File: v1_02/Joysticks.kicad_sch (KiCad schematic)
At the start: 29 parts, among them J10 DB9_Male_MountingHoles, J11 DA15_Socket_MountingHoles, J13 Aliexpress ADS1115 module, J15 Conn_01x01_Pin, J17 Conn_01x03_Pin, U4 74LV165A, U5 74LV165A, U6 LM4040D20ILPR, U7 PCF8583T, Y1 32.768 kHz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

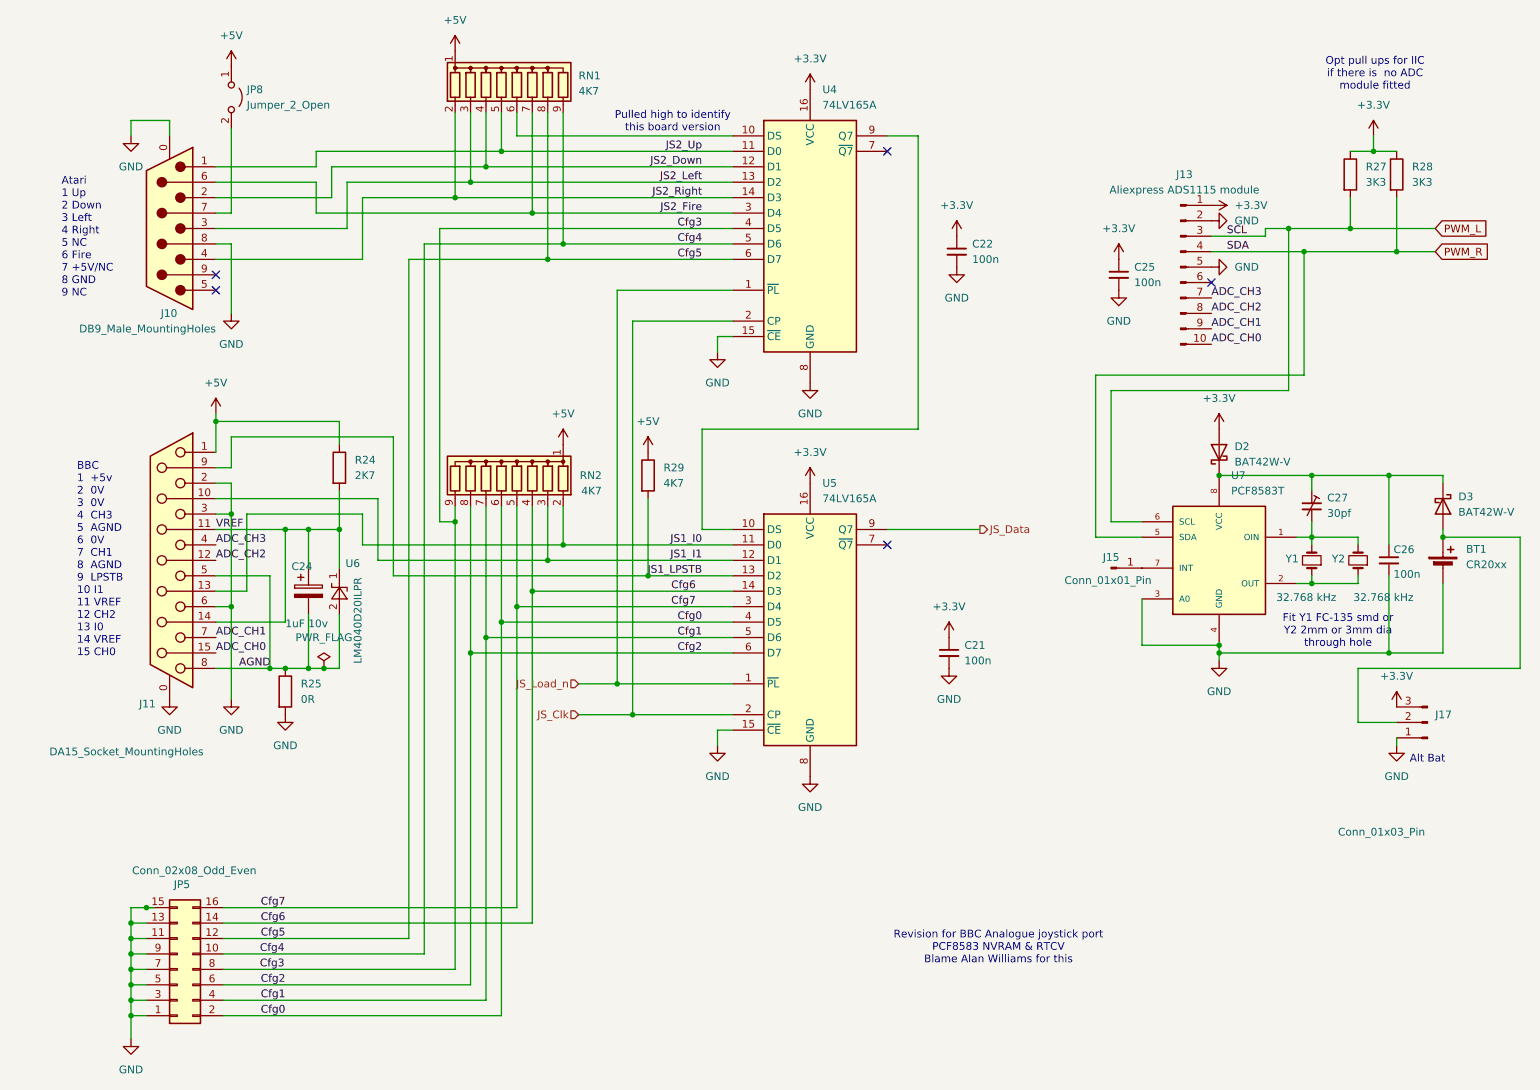
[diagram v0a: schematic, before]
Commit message: v1_02: Fix some ERC warnings
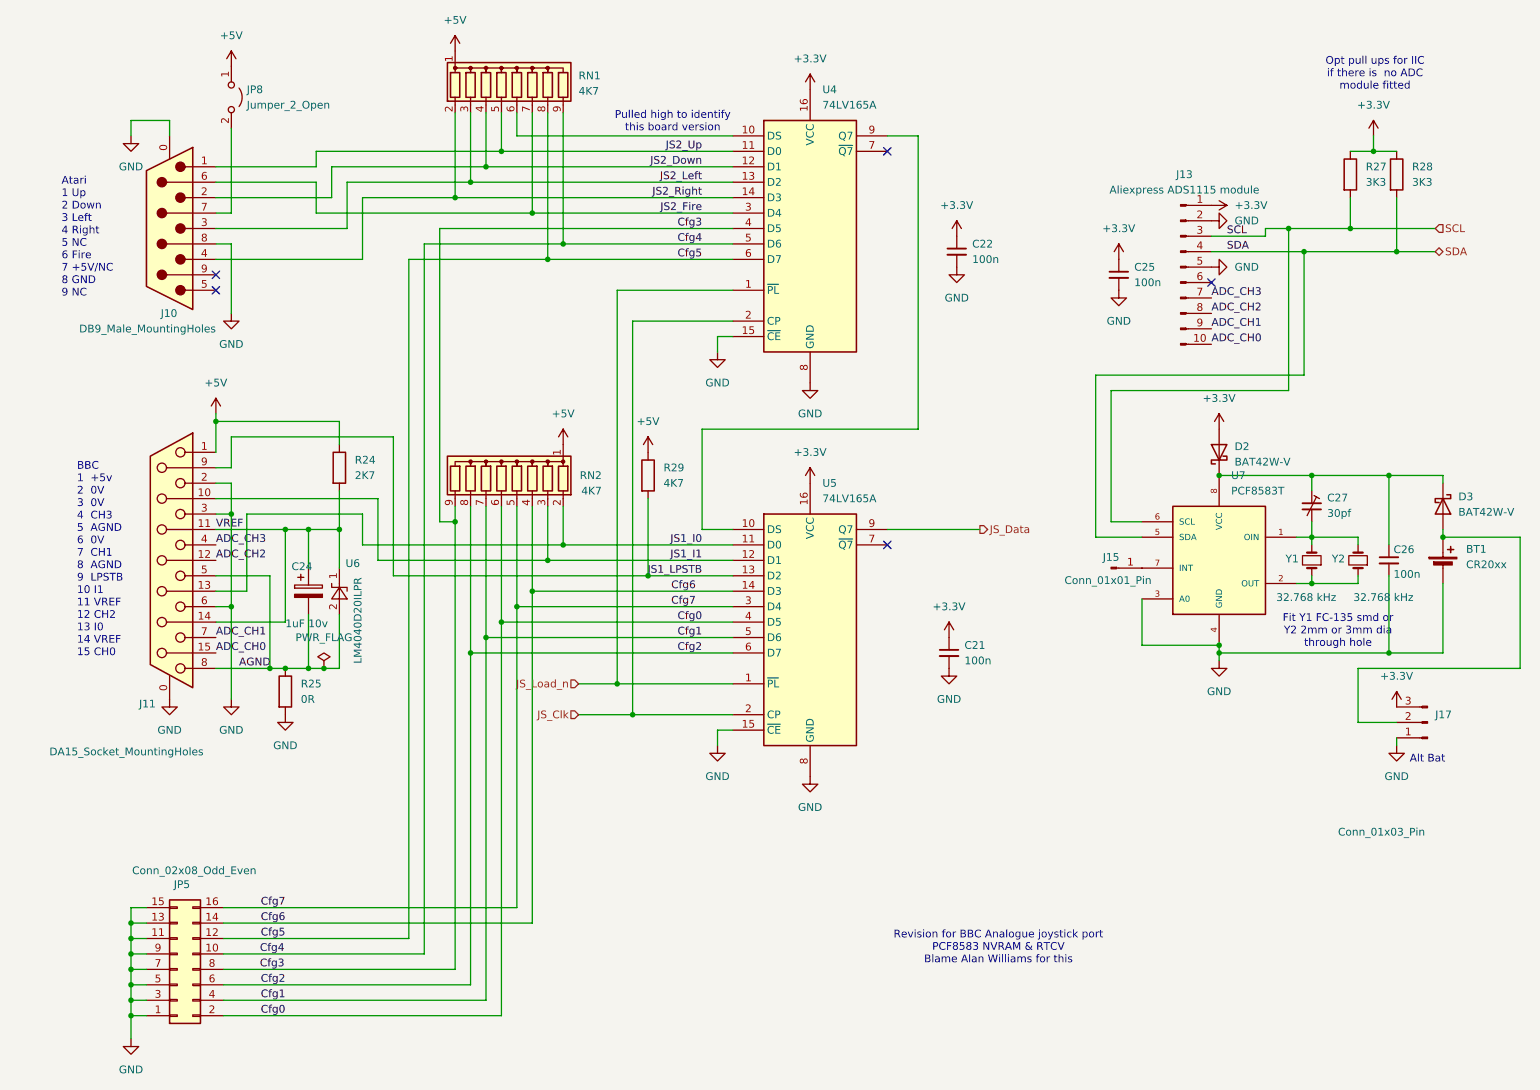
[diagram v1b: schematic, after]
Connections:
- net AGND: now reaches C24.2, J11.5, J11.8, R25.1, U6.2 (A)
- net PWM_L renamed SCL
- net PWM_R renamed SDA
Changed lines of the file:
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@@
+	)
+	(junction
+		(at 248.92 110.49)
+		(diameter 0)
+		(color 0 0 0 0)
+	)
+	(junction
+		(at 134.62 127)
+		(diameter 0)
+		(color 0 0 0 0)
+	)
+	(junction
+		(at 125.73 104.14)
+		(diameter 0)
+		(color 0 0 0 0)
+	)
+	(junction
+		(at 86.36 124.46)
+		(diameter 0)
+		(color 0 0 0 0)
+	)
+	(junction
+		(at 71.12 114.3)
+		(diameter 0)
+		(color 0 0 0 0)
+	)
+	(junction
+		(at 120.65 49.53)
+		(diameter 0)
+		(color 0 0 0 0)
+	)
+	(junction
+		(at 107.95 46.99)
+		(diameter 0)
+		(color 0 0 0 0)
+	)
+	(junction
+		(at 137.16 132.08)
+		(diameter 0)
+		(color 0 0 0 0)
 	)
 	(junction
@@
 	)
 	(junction
-		(at 248.92 110.49)
-		(diameter 0)
-		(color 0 0 0 0)
-	)
-	(junction
-		(at 134.62 127)
-		(diameter 0)
-		(color 0 0 0 0)
-	)
-	(junction
-		(at 125.73 104.14)
-		(diameter 0)
-		(color 0 0 0 0)
-	)
-	(junction
-		(at 86.36 124.46)
-		(diameter 0)
-		(color 0 0 0 0)
-	)
-	(junction
-		(at 71.12 114.3)
-		(diameter 0)
-		(color 0 0 0 0)
-	)
-	(junction
-		(at 120.65 49.53)
-		(diameter 0)
-		(color 0 0 0 0)
-	)
-	(junction
-		(at 107.95 46.99)
-		(diameter 0)
-		(color 0 0 0 0)
-	)
-	(junction
-		(at 137.16 132.08)
-		(diameter 0)
-		(color 0 0 0 0)
-	)
-	(junction
 		(at 54.61 181.61)
 		(diameter 0)
@@
 	(junction
 		(at 54.61 176.53)
-		(diameter 0)
-		(color 0 0 0 0)
-	)
-	(junction
-		(at 57.15 163.83)
 		(diameter 0)
 		(color 0 0 0 0)
@@
 	(wire
 		(pts
+			(xy 68.58 124.46) (xy 77.47 124.46)
+		)
+		(stroke
+			(width 0)
+			(type default)
+		)
+	)
+	(wire
+		(pts
 			(xy 107.95 97.79) (xy 107.95 100.33)
 		)
@@
 	(wire
 		(pts
-			(xy 68.58 124.46) (xy 77.47 124.46)
-		)
-		(stroke
-			(width 0)
-			(type default)
-		)
-	)
-	(wire
-		(pts
 			(xy 69.85 176.53) (xy 110.49 176.53)
 		)
@@
 		(pts
 			(xy 125.73 104.14) (xy 153.67 104.14)
-		)
-		(stroke
-			(width 0)
-			(type default)
-		)
-	)
-	(wire
-		(pts
-			(xy 58.42 163.83) (xy 57.15 163.83)
 		)
 		(stroke
@@
 		)
 	)
-	(label ""
-		(at 81.28 124.46 0)
-		(effects
-			(font
-				(size 1.27 1.27)
-			)
-			(justify left bottom)
-		)
-	)
 	(label "Cfg0"
 		(at 80.01 181.61 180)
@@
 			)
 			(justify right bottom)
-		)
-	)
-	(global_label "PWM_R"
-		(shape input)
-		(at 269.24 55.88 0)
-		(fields_autoplaced yes)
-		(effects
-			(font
-				(size 1.27 1.27)
-			)
-			(justify left)
-		)
-		(property "Intersheetrefs" "${INTERSHEET_REFS}"
-			(at 278.6356 55.88 0)
-			(effects
-				(font
-					(size 1.27 1.27)
-				)
-				(justify left)
-				(hide yes)
-			)
-		)
-	)
-	(global_label "PWM_L"
-		(shape input)
-		(at 269.24 52.07 0)
-		(fields_autoplaced yes)
-		(effects
-			(font
-				(size 1.27 1.27)
-			)
-			(justify left)
-		)
-		(property "Intersheetrefs" "${INTERSHEET_REFS}"
-			(at 278.3937 52.07 0)
-			(effects
-				(font
-					(size 1.27 1.27)
-				)
-				(justify left)
-				(hide yes)
-			)
 		)
 	)
@@
 		)
 	)
+	(hierarchical_label "SDA"
+		(shape bidirectional)
+		(at 269.24 55.88 0)
+		(effects
+			(font
+				(size 1.27 1.27)
+			)
+			(justify left)
+		)
+	)
 	(hierarchical_label "JS_Clk"
 		(shape input)
@@
 		)
 	)
+	(hierarchical_label "SCL"
+		(shape input)
+		(at 269.24 52.07 0)
+		(effects
+			(font
+				(size 1.27 1.27)
+			)
+			(justify left)
+		)
+	)

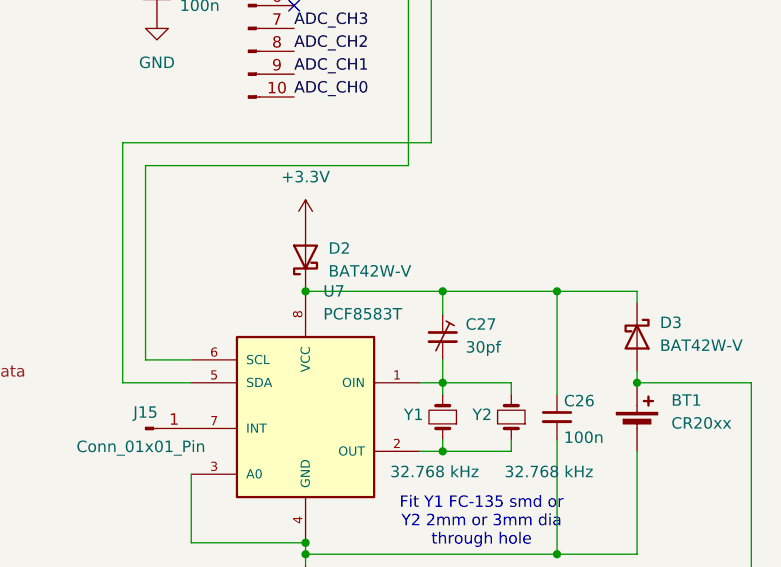
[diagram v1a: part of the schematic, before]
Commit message: v1_02: Updated symbols/footprints for KiCAD9; fix all ERC/DRC warnings
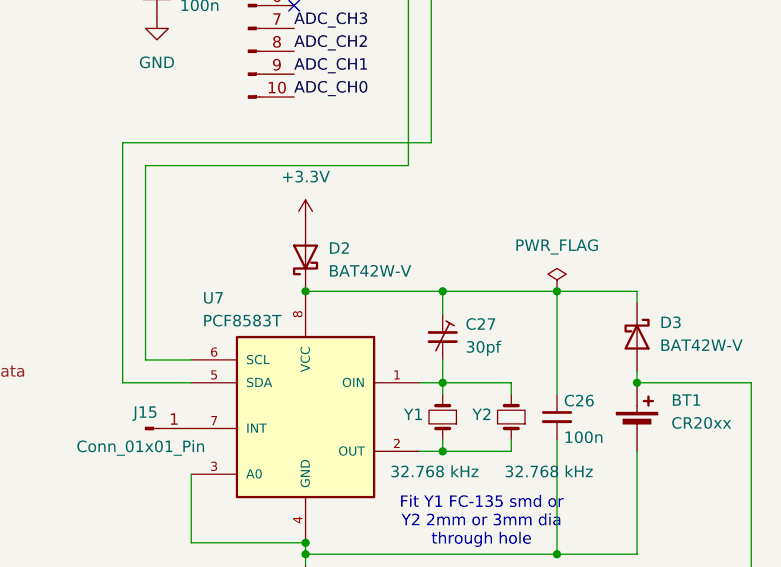
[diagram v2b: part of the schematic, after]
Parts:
- J10: symbol Connector:DB9_Male_MountingHoles -> Connector:DE9_Pins_MountingHoles
- U7: symbol PCF8583:PCF8583 -> TangNano20k:PCF8583
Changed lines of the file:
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@@
 			)
 		)
-		(property "Description" ""
+		(property "Description" "Power symbol creates a global label with name \"GND\" , ground"
 			(at 166.37 142.24 0)
 			(effects
@@
 			)
 		)
-		(property "Description" ""
+		(property "Description" "Power symbol creates a global label with name \"GND\" , ground"
 			(at 80.01 132.08 0)
 			(effects
@@
 			)
 		)
-		(property "Description" ""
+		(property "Description" "Power symbol creates a global label with name \"GND\" , ground"
 			(at 60.96 129.54 0)
 			(effects
@@
 			)
 		)
-		(property "Description" ""
+		(property "Description" "Power symbol creates a global label with name \"+3.3V\""
 			(at 262.89 130.81 0)
 			(effects
@@
 			)
 		)
-		(property "Description" ""
+		(property "Description" "Power symbol creates a global label with name \"GND\" , ground"
 			(at 262.89 137.16 0)
 			(effects
@@
 			)
 		)
-		(property "Description" ""
+		(property "Description" "Power symbol creates a global label with name \"+3.3V\""
 			(at 217.17 57.15 0)
 			(effects
@@
 			)
 		)
-		(property "Description" ""
+		(property "Description" "Power symbol creates a global label with name \"GND\" , ground"
 			(at 233.68 123.19 0)
 			(effects
@@
 			)
 		)
-		(property "Description" ""
+		(property "Description" "Power symbol creates a global label with name \"GND\" , ground"
 			(at 151.13 72.39 0)
 			(effects
@@
 			)
 		)
-		(property "Description" ""
+		(property "Description" "Power symbol creates a global label with name \"+5V\""
 			(at 71.12 25.4 0)
 			(effects
@@
 			)
 		)
-		(property "Description" ""
+		(property "Description" "Power symbol creates a global label with name \"+3.3V\""
 			(at 166.37 93.98 0)
 			(effects
@@
 			)
 		)
-		(property "Description" ""
+		(property "Description" "Power symbol creates a global label with name \"+3.3V\""
 			(at 259.08 36.83 0)
 			(effects
@@
 			)
 		)
-		(property "Description" ""
+		(property "Description" "Power symbol creates a global label with name \"GND\" , ground"
 			(at 232.41 50.8 0)
 			(effects
@@
 			)
 		)
-		(property "Description" ""
+		(property "Description" "Power symbol creates a global label with name \"+3.3V\""
 			(at 232.41 48.26 0)
 			(effects
@@
 			)
 		)
-		(property "Description" ""
+		(property "Description" "Power symbol creates a global label with name \"GND\" , ground"
 			(at 232.41 58.42 0)
 			(effects
@@
 			)
 		)
-		(property "Description" ""
+		(property "Description" "Power symbol creates a global label with name \"+3.3V\""
 			(at 166.37 29.21 0)
 			(effects
@@
 			)
 		)
-		(property "Description" ""
+		(property "Description" "Power symbol creates a global label with name \"GND\" , ground"
 			(at 54.61 185.42 0)
 			(effects
@@
 			)
 		)
-		(property "Description" ""
+		(property "Description" "Power symbol creates a global label with name \"+3.3V\""
 			(at 190.5 53.34 0)
 			(effects
@@
 			)
 		)
-		(property "Description" ""
+		(property "Description" "Power symbol creates a global label with name \"GND\" , ground"
 			(at 217.17 62.23 0)
 			(effects
@@
 			)
 		)
-		(property "Description" ""
+		(property "Description" "Power symbol creates a global label with name \"GND\" , ground"
 			(at 71.12 129.54 0)
 			(effects
@@
 			)
 		)
-		(property "Description" ""
+		(property "Description" "Power symbol creates a global label with name \"+5V\""
 			(at 139.7 88.9 0)
 			(effects
@@
 			)
 		)
-		(property "Description" ""
+		(property "Description" "Power symbol creates a global label with name \"+3.3V\""
 			(at 189.23 119.38 0)
 			(effects
@@
 			)
 		)
-		(property "Description" ""
+		(property "Description" "Power symbol creates a global label with name \"GND\" , ground"
 			(at 189.23 124.46 0)
 			(effects
@@
 			)
 		)
-		(property "Description" ""
+		(property "Description" "Power symbol creates a global label with name \"GND\" , ground"
 			(at 151.13 137.16 0)
 			(effects
@@
 			)
 		)
-		(property "Description" ""
+		(property "Description" "Power symbol creates a global label with name \"+5V\""
 			(at 68.58 82.55 0)
 			(effects
@@
 	)
 	(symbol
+		(lib_id "power:PWR_FLAG")
+		(at 261.62 92.71 0)
+		(unit 1)
+		(exclude_from_sim no)
+		(in_bom yes)
+		(on_board yes)
+		(dnp no)
+		(fields_autoplaced yes)
+		(property "Reference" "#FLG02"
+			(at 261.62 90.805 0)
+			(effects
+				(font
+					(size 1.27 1.27)
+				)
+				(hide yes)
+			)
+		)
+		(property "Value" "PWR_FLAG"
+			(at 261.62 87.63 0)
+			(effects
+				(font
+					(size 1.27 1.27)
+				)
+			)
+		)
+		(property "Footprint" ""
+			(at 261.62 92.71 0)
+			(effects
+				(font
+					(size 1.27 1.27)
+				)
+				(hide yes)
+			)
+		)
+		(property "Datasheet" "~"
+			(at 261.62 92.71 0)
+			(effects
+				(font
+					(size 1.27 1.27)
+				)
+				(hide yes)
+			)
+		)
+		(property "Description" "Special symbol for telling ERC where power comes from"
+			(at 261.62 92.71 0)
+			(effects
+				(font
+					(size 1.27 1.27)
+				)
+				(hide yes)
+			)
+		)
+		(pin "1"
+		)
+		(instances
+			(project ""
+				(path "/db04e0fc-671d-454e-9fa2-9bb21001ea6b/0331ec4d-b3bf-4145-9efb-ad1204df77fa"
+					(reference "#FLG02")
+					(unit 1)
+				)
+			)
+		)
+	)
+	(symbol
 		(lib_id "Connector:Conn_01x01_Pin")
 		(at 215.9 107.95 0)
@@
 			)
 		)
-		(property "Description" ""
+		(property "Description" "Power symbol creates a global label with name \"+5V\""
 			(at 107.95 22.86 0)
 			(effects
@@
 	)
 	(symbol
-		(lib_id "Connector:DB9_Male_MountingHoles")
+		(lib_id "Connector:DE9_Pins_MountingHoles")
 		(at 60.96 52.07 180)
 		(unit 1)
@@
 			)
 		)
-		(property "Description" ""
+		(property "Description" "9-pin D-SUB connector, pins (male), Mounting Hole"
 			(at 60.96 52.07 0)
 			(effects
@@
 			)
 		)
-		(property "Description" ""
+		(property "Description" "Power symbol creates a global label with name \"GND\" , ground"
 			(at 166.37 77.47 0)
 			(effects
@@
 			)
 		)
-		(property "Description" ""
+		(property "Description" "Power symbol creates a global label with name \"GND\" , ground"
 			(at 190.5 58.42 0)
 			(effects
@@
 			)
 		)
-		(property "Description" ""
+		(property "Description" "Power symbol creates a global label with name \"+5V\""
 			(at 125.73 87.63 0)
 			(effects
@@
 			)
 		)
-		(property "Description" ""
+		(property "Description" "Power symbol creates a global label with name \"GND\" , ground"
 			(at 54.61 36.83 0)
 			(effects
@@
 			)
 		)
-		(property "Description" ""
+		(property "Description" "Power symbol creates a global label with name \"GND\" , ground"
 			(at 71.12 66.04 0)
 			(effects
@@
 			)
 		)
-		(property "Description" ""
+		(property "Description" "Power symbol creates a global label with name \"+3.3V\""
 			(at 233.68 85.09 0)
 			(effects
@@
 	)
 	(symbol
-		(lib_id "PCF8583:PCF8583")
+		(lib_id "TangNano20k:PCF8583")
 		(at 233.68 105.41 0)
 		(unit 1)
@@
 		(on_board yes)
 		(dnp no)
-		(fields_autoplaced yes)
 		(property "Reference" "U7"
-			(at 235.6486 92.71 0)
+			(at 222.25 93.472 0)
 			(effects
 				(font
@@
 		)
 		(property "Value" "PCF8583T"
-			(at 235.6486 95.25 0)
+			(at 222.25 96.012 0)
 			(effects
 				(font
